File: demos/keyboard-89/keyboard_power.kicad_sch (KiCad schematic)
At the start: 3 parts, among them J1 USBC, U2 LDO

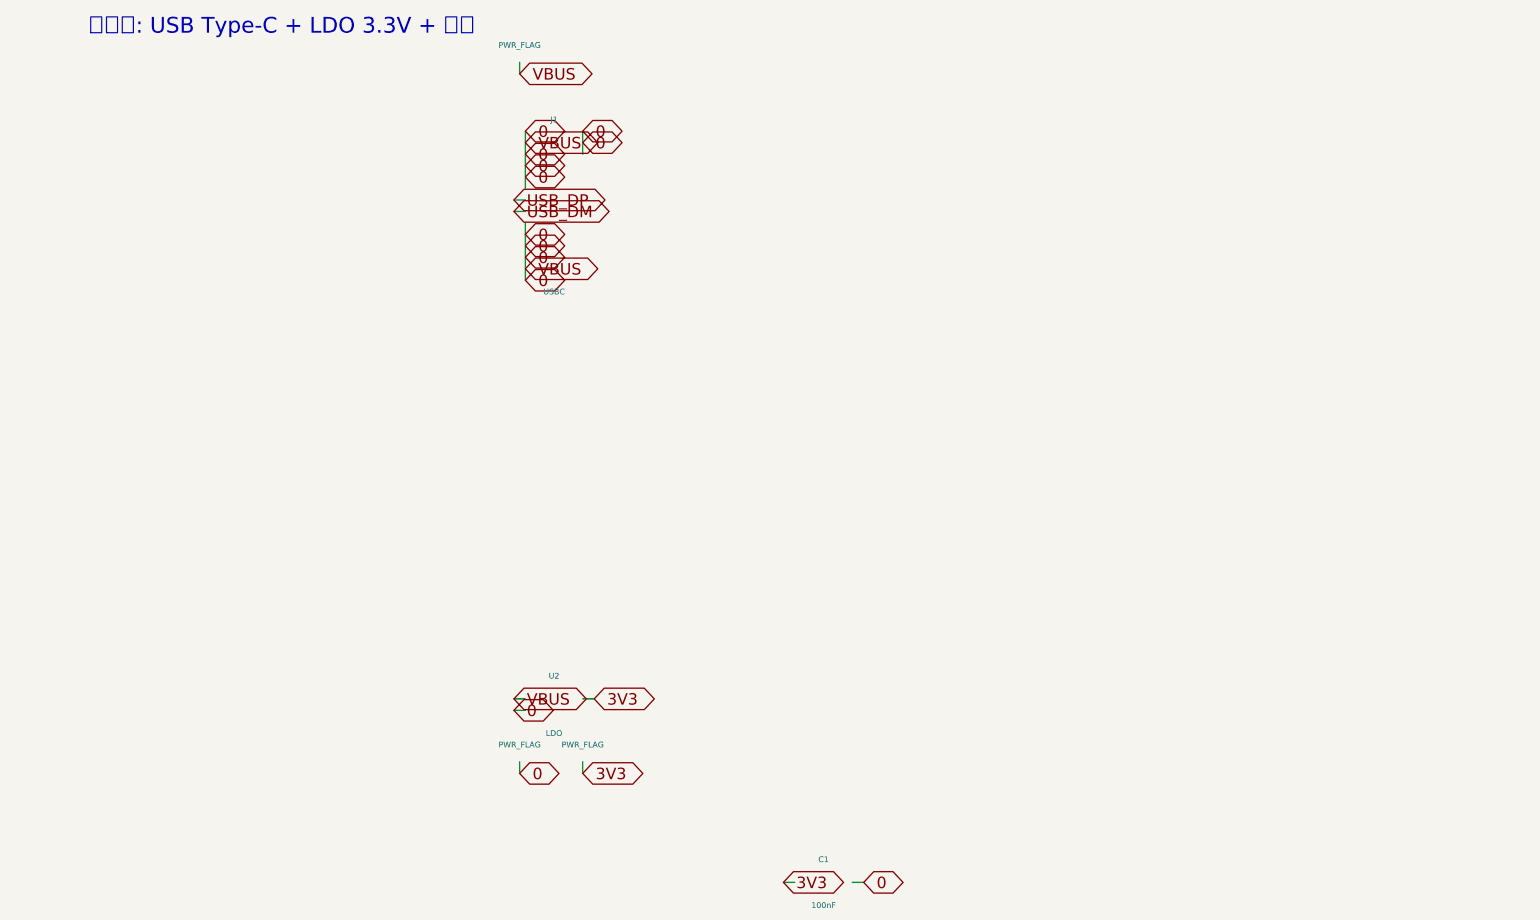
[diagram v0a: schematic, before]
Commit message: fix: update default label height in kicad_sch_add_label function to 1.27mm
feat: add redraw_kb89.py script for redrawing keyboard-89 schematic with new tools
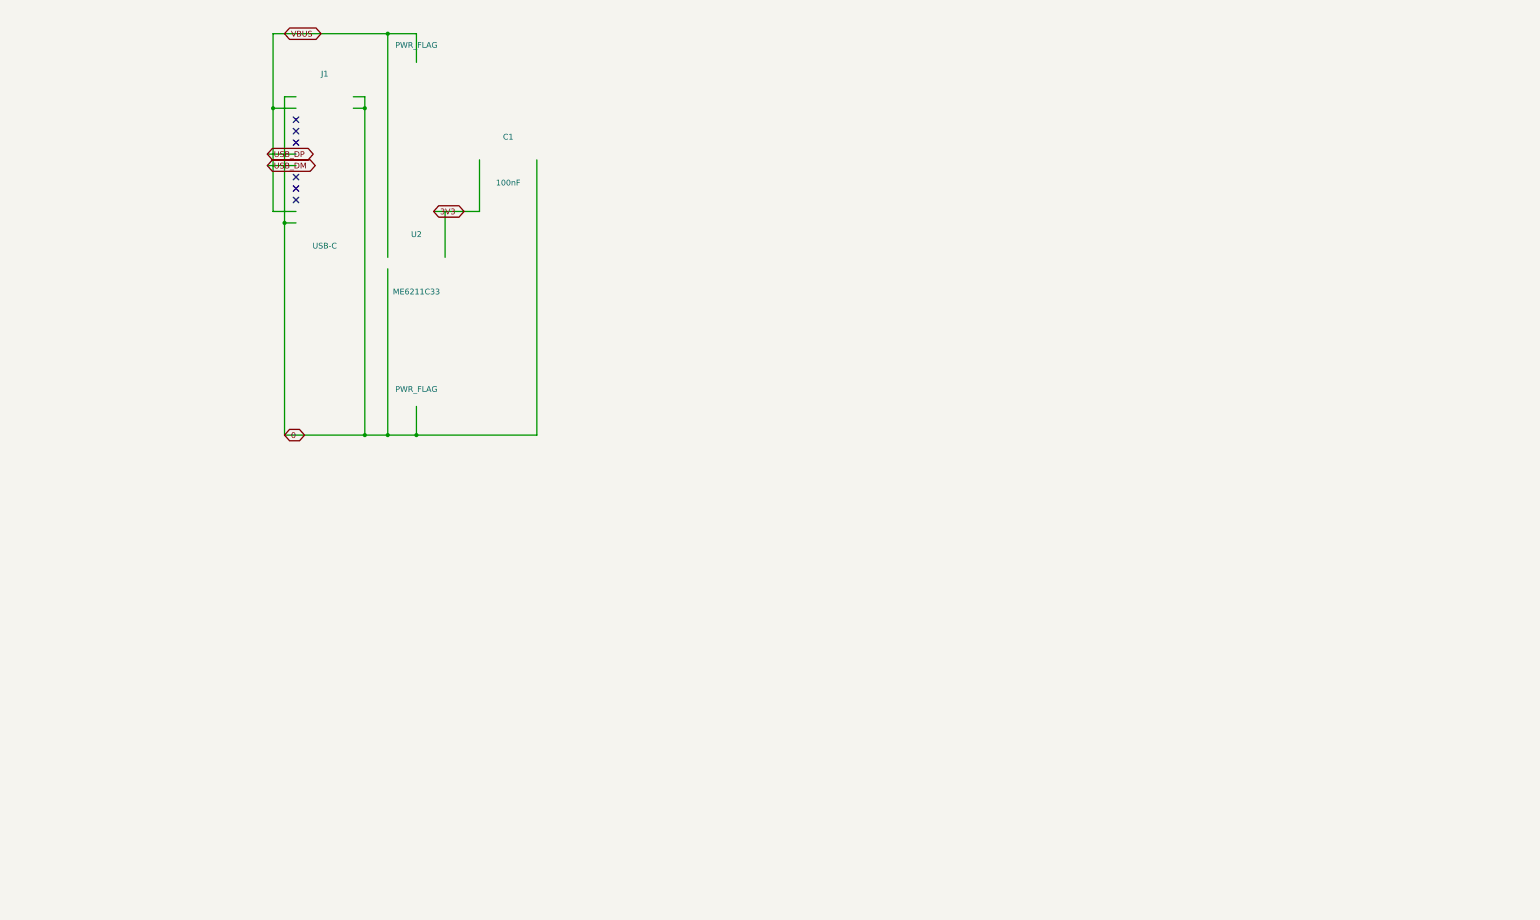
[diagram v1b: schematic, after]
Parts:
- J1: value USBC -> USB-C
- U2: value LDO -> ME6211C33
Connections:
- net 0: no longer J1.10 (CC2), J1.11 (VBUS), J1.2 (VBUS), J1.3 (SBU2), J1.4 (CC1), J1.5 (DN2), J1.8 (DP2), J1.9 (SBU1), U2.3 (VIN)
- new net VBUS: J1.11 (VBUS), J1.2 (VBUS), U2.3 (VIN)
- no-connect marks 0 -> 6
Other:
- note removed: "电源页: USB Type-C + LDO 3.3V + 去耦"

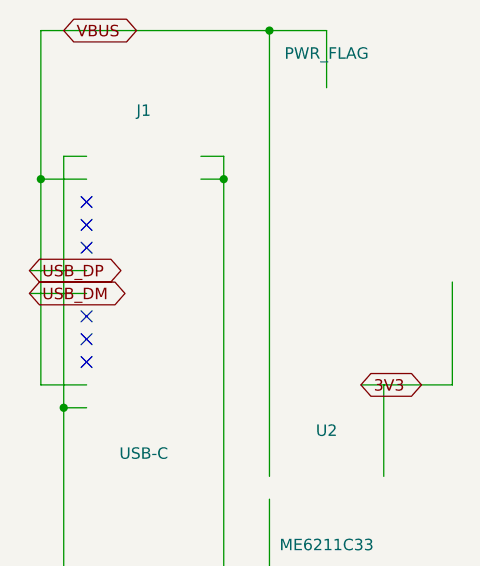
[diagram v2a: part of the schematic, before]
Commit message: feat: add overlap checking and auto repositioning tools
- Introduced a new module for checking and fixing overlaps and out-of-bounds elements in schematic designs.
- Implemented functions to read existing wires and check for overlaps between symbols and labels.
- Enhanced label placement logic to avoid collisions with existing wires.
- Updated the circuit drawing function to utilize the new overlap checking features.
- Modified the redraw tests to accommodate changes in label spacing and positioning.
- Added new tools to the main tools list for easy access.
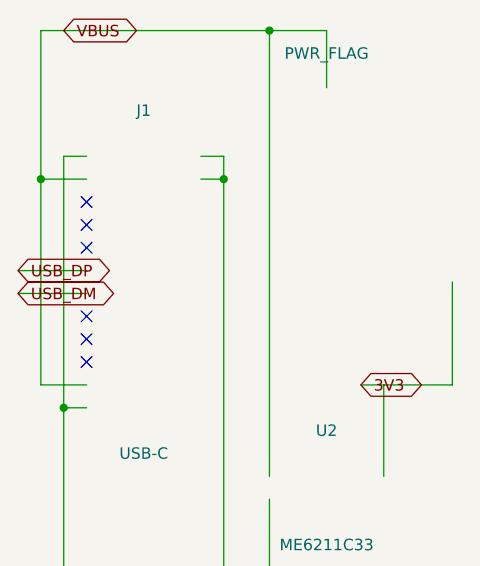
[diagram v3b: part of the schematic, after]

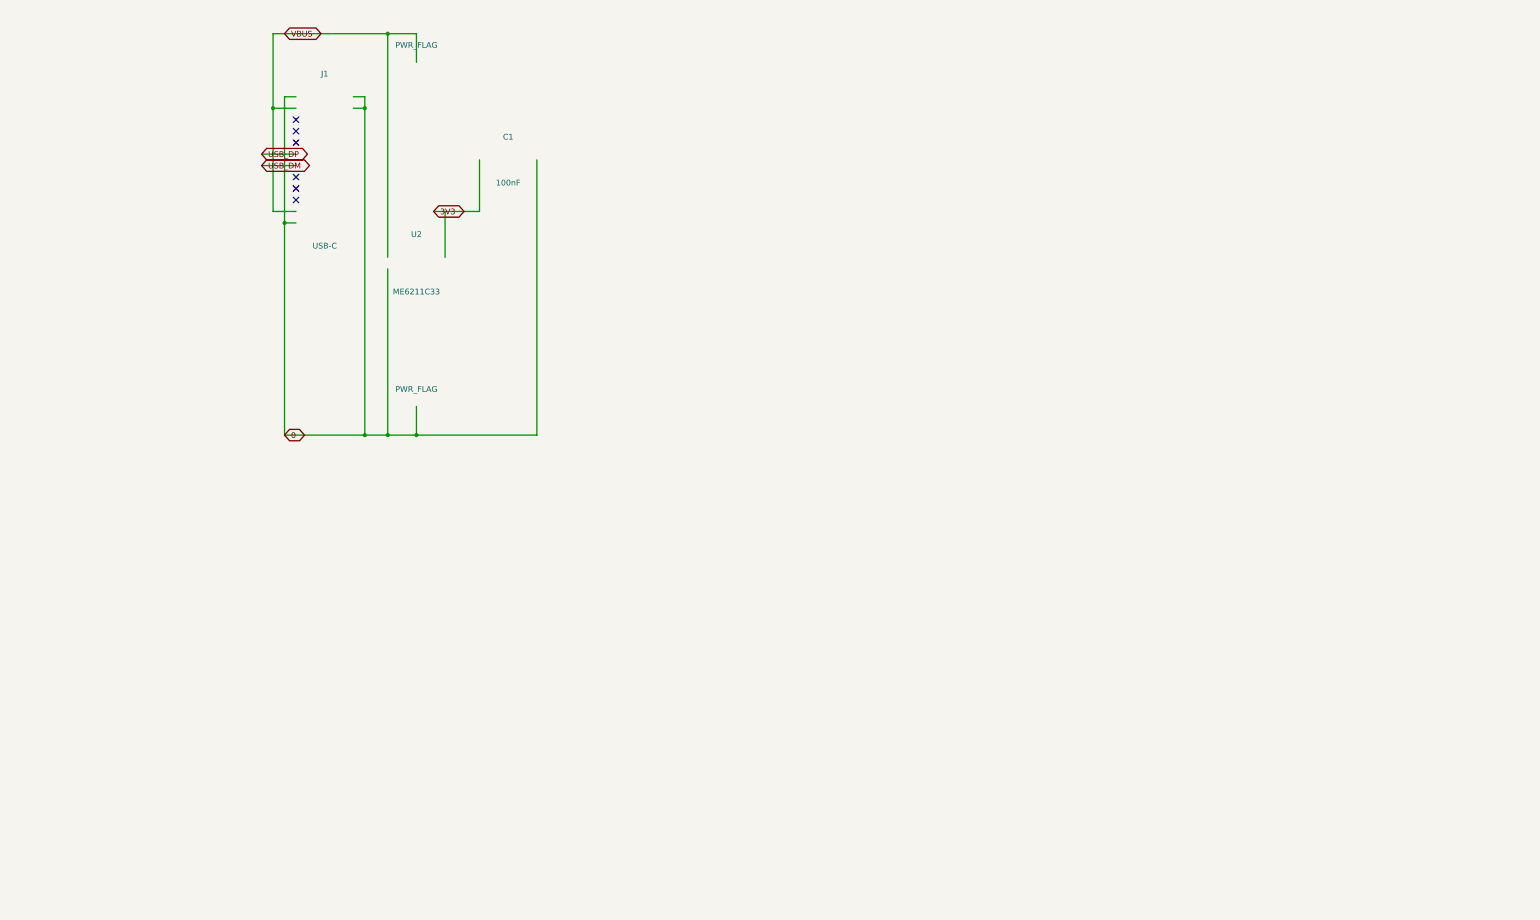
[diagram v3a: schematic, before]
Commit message: Add ERC report, AI setup documentation, and bootstrap scripts
- Created a new ERC report for the keyboard-89 project detailing isolated pin labels and library issues.
- Added AI environment bootstrap documentation for setting up the development environment on Windows and Linux.
- Implemented a PowerShell bootstrap script for Windows to automate the setup of dependencies, environment, and build process.
- Developed a corresponding bash bootstrap script for Linux with similar functionality.
- Introduced a new test for verifying pin connections in the symbol writer module.
- Added JSON report for failed drawing processes with a specific error message in Chinese.
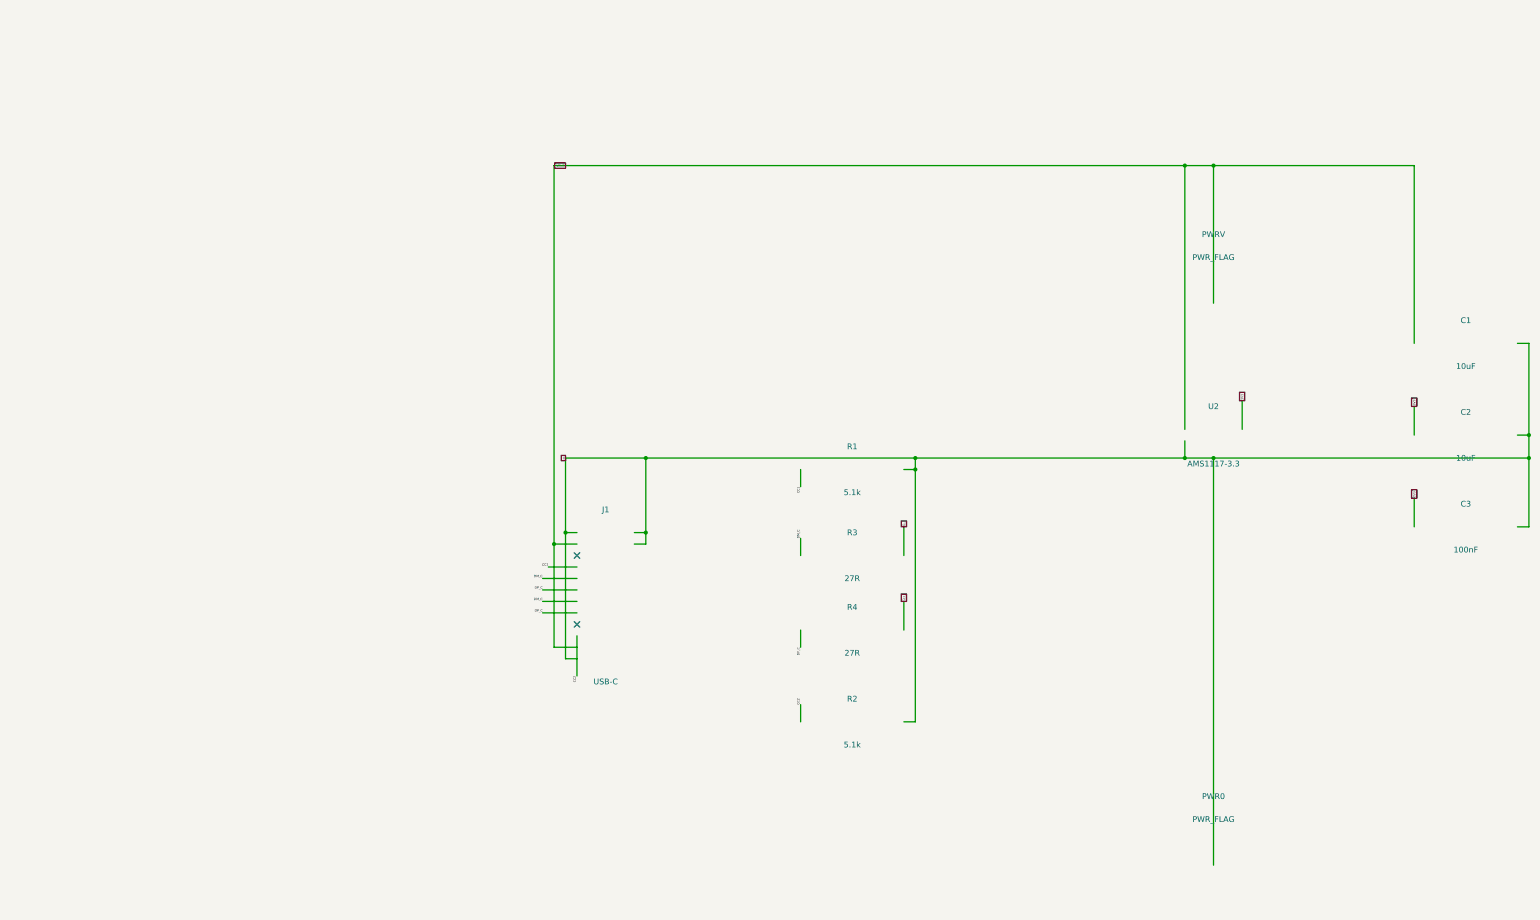
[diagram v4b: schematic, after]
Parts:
- removed C1: 100nF, Capacitor_SMD:C_0402_1005Metric, symbol keyboard-89_local:C-100nF
- added C1, C2: 10uF, keyboard-89_local:C_0805_2012Metric, symbol keyboard-89_local:C_GENERIC
- added C3: 100nF, keyboard-89_local:C_0402_1005Metric, symbol keyboard-89_local:C_GENERIC
- added PWR0, PWRV: PWR_FLAG, symbol keyboard-89_local:POWER_FLAG
- added R1, R2: 5.1k, keyboard-89_local:R_0402_1005Metric, symbol keyboard-89_local:R_GENERIC
- added R3, R4: 27R, keyboard-89_local:R_0402_1005Metric, symbol keyboard-89_local:R_GENERIC
- J1: footprint (none) -> keyboard-89_local:USB_C_16P_2MD_073
- U2: value ME6211C33 -> AMS1117-3.3; footprint (none) -> keyboard-89_local:SOT-89-3
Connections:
- net USB_DM is gone; now on net DM_C: J1.7 (DN1)
- net USB_DP is gone; now on net DP_C: J1.6 (DP1)
- net 0: now also C1.2, C2.2, C3.2, PWR0.1 (pwr), R1.2, R2.2
- net 3V3: now also C2.1, C3.1
- net VBUS: now also C1.1, PWRV.1 (pwr)
- net CC2: now reaches J1.10 (CC2)
- net CC2: now also R2.1
- net CC1: now reaches J1.4 (CC1)
- net CC1: now also R1.1
- net DM_C: now reaches J1.5 (DN2)
- net DM_C: now also R3.1
- net DP_C: now reaches J1.8 (DP2)
- net DP_C: now also R4.1
- new net D+: R4.2
- new net D-: R3.2
- no-connect marks 6 -> 2
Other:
- company: (none) -> Keyboard-89
- title: keyboard_power -> Keyboard-89 USB-C and Power
